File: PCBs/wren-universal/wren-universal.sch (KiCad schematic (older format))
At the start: 117 parts, among them J1 TRRS_Jack, SW0 Reset, U1 Elite-C

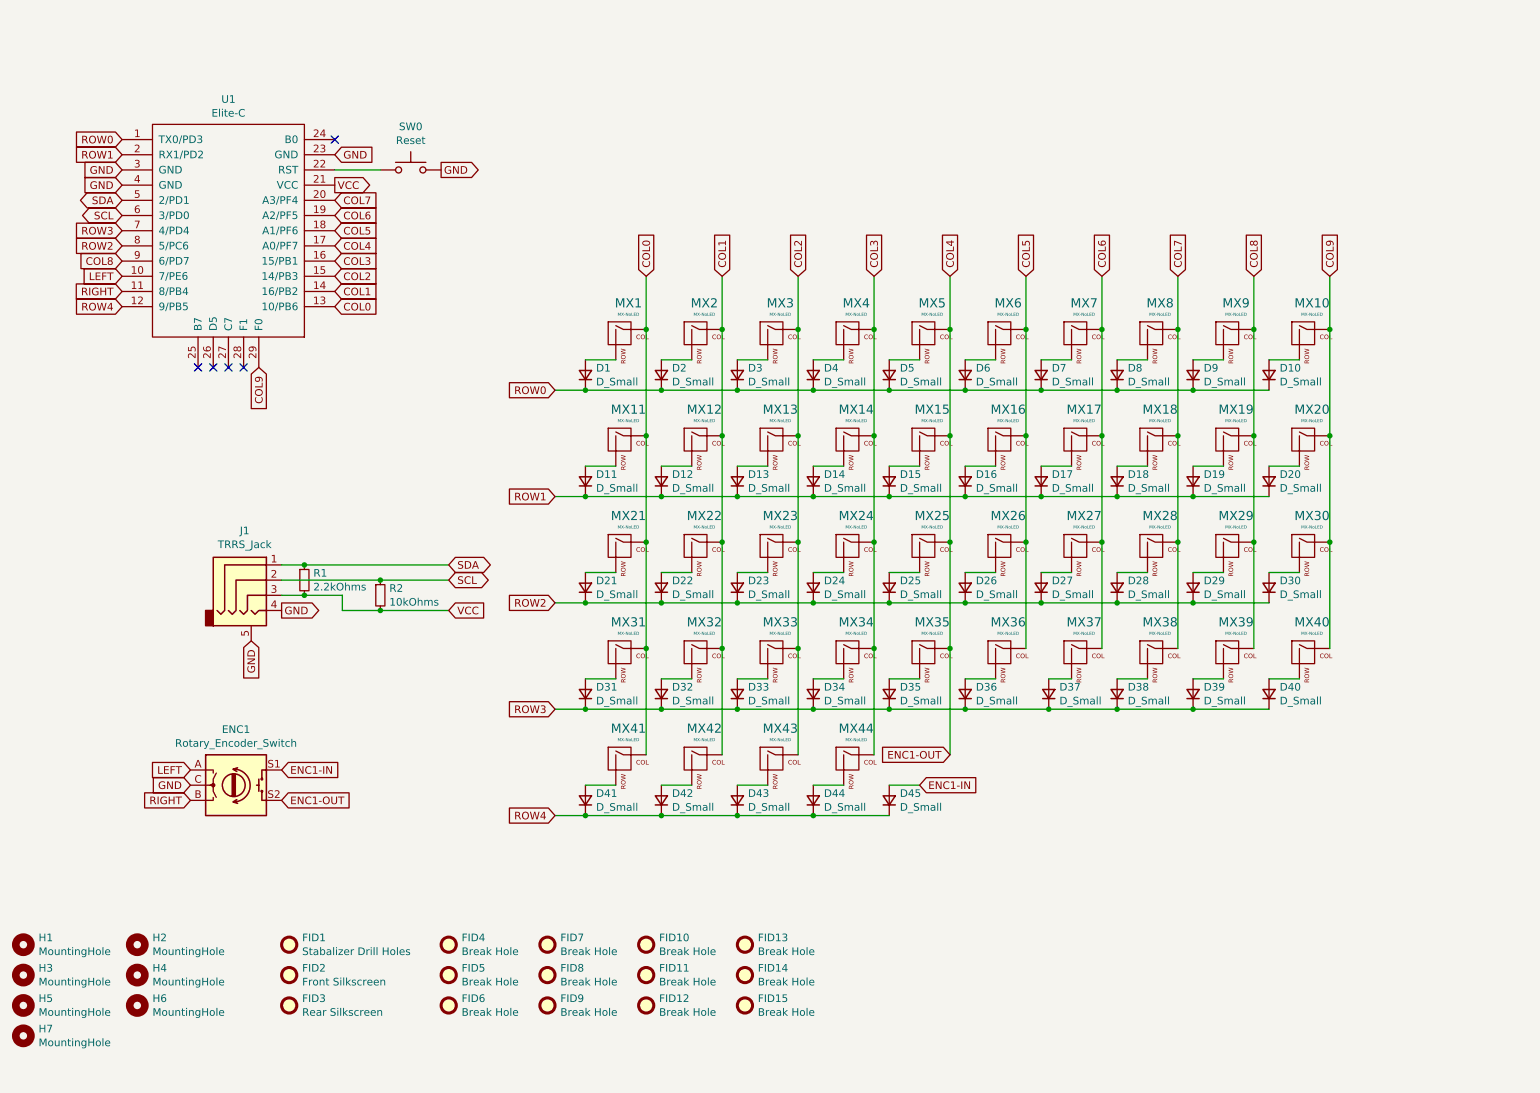
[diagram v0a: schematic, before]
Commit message: Add Egg detachable macro pad
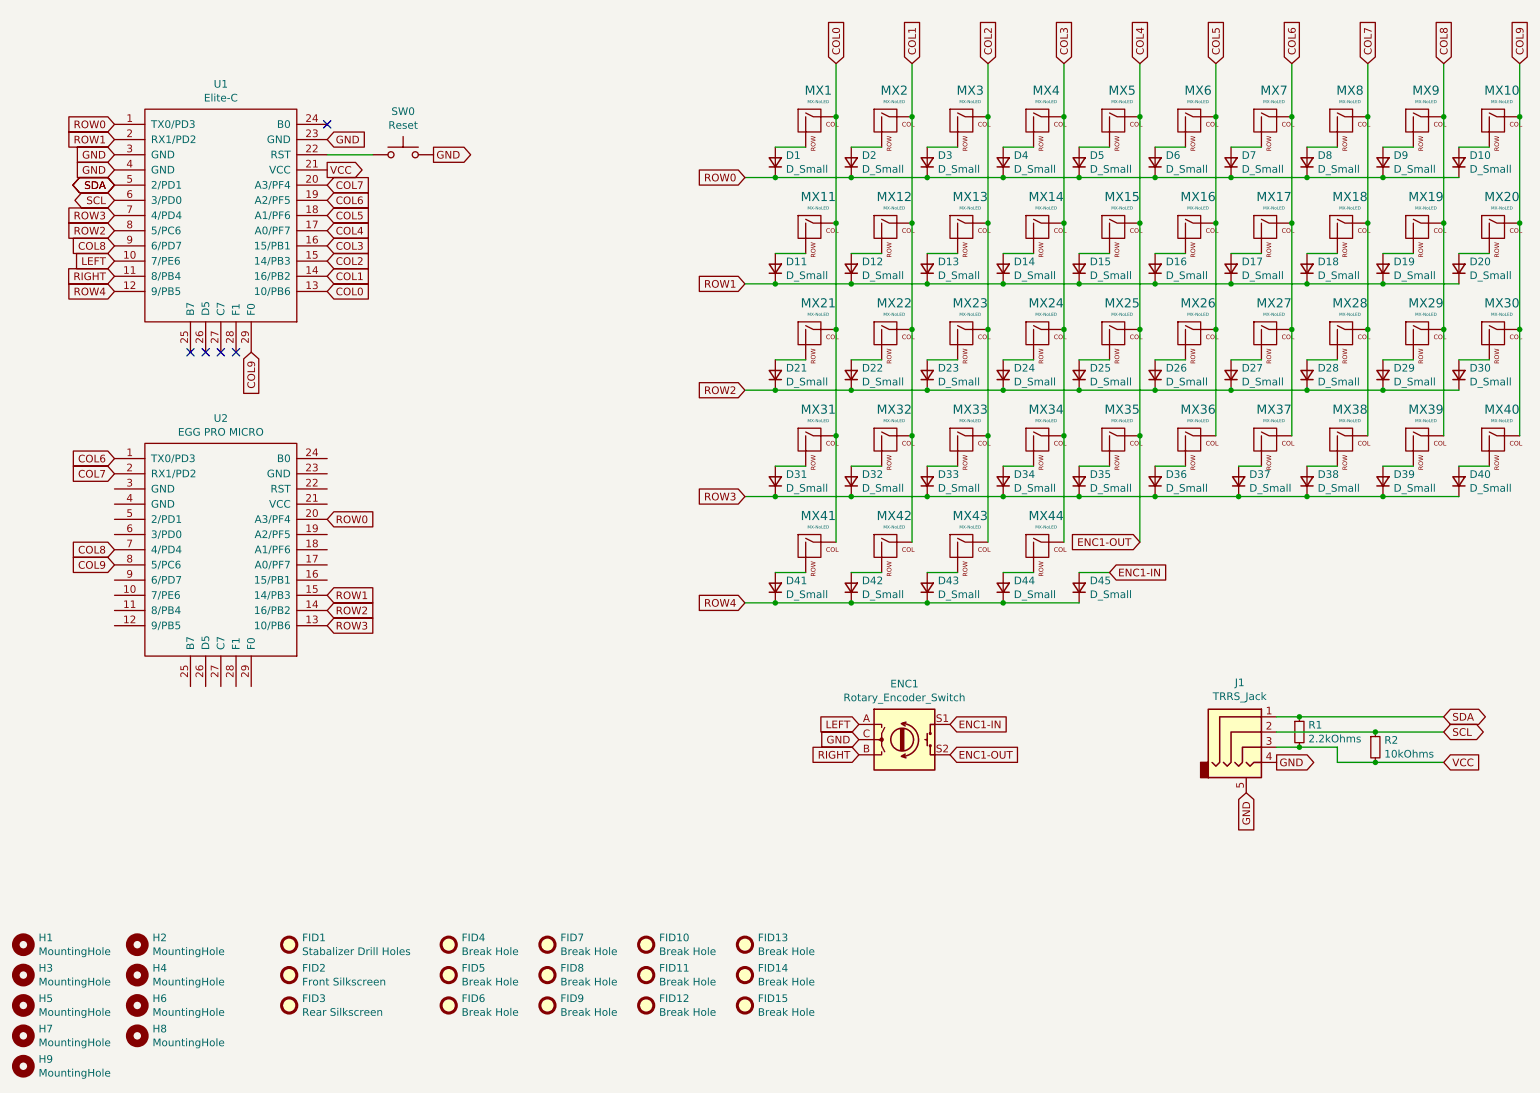
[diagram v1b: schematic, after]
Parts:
- added H8, H9: MountingHole, MountingHole:MountingHole_5.5mm, symbol Mechanical:MountingHole
- added U2: EGG PRO MICRO, footprints:ARDUINO_PRO_MICRO, symbol wren-numpad-rescue:Elite-C-keebio-wren-left-rescue
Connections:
- net COL6: now also U2.1 (TX0/PD3)
- net COL7: now also U2.2 (RX1/PD2)
- net COL8: now also U2.7 (4/PD4)
- net COL9: now also U2.8 (5/PC6)
- net ROW0: now also U2.20 (A3/PF4)
- net ROW1: now also U2.15 (14/PB3)
- net ROW2: now also U2.14 (16/PB2)
- net ROW3: now also U2.13 (10/PB6)
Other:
- moved on the sheet: D1, D10, D11, D12, D13, D14, D15, D16, D17, D18, D19, D2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

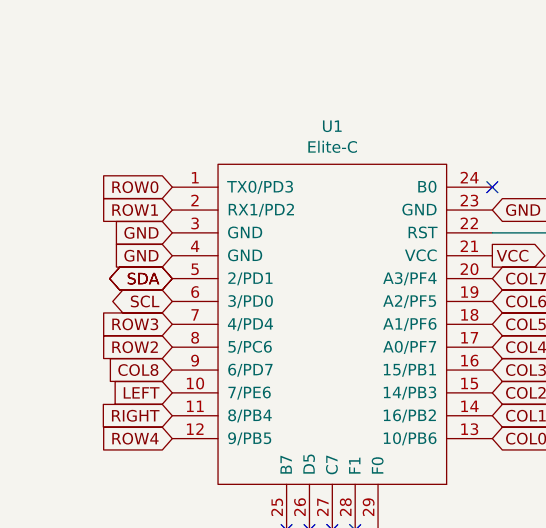
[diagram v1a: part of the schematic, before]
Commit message: Clean up design rules, traces.
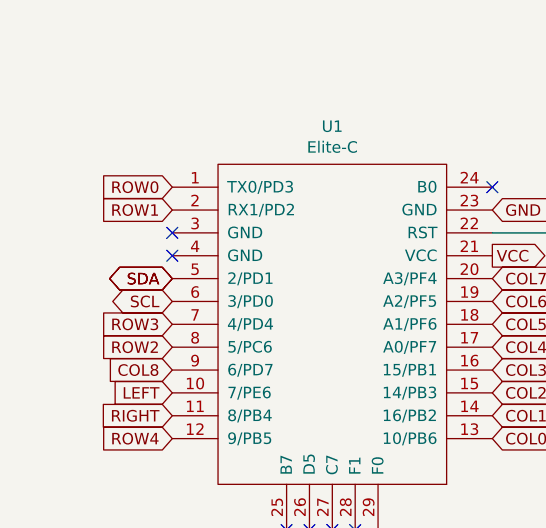
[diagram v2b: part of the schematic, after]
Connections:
- net GND: no longer U1.3 (GND), U1.4 (GND)
- no-connect marks 5 -> 7
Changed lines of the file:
@@
 Text GLabel 2650 2850 3    50   Input ~ 0
 COL9
-Text GLabel 1750 1550 0    50   Input ~ 0
-GND
-Text GLabel 1750 1650 0    50   Input ~ 0
-GND
 NoConn ~ 2350 2850
 NoConn ~ 2250 2850
@@
 Text GLabel 3150 4650 2    50   Input ~ 0
 ROW3
+NoConn ~ 1750 1550
+NoConn ~ 1750 1650
 $EndSCHEMATC
